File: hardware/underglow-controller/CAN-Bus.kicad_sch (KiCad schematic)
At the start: 4 parts, among them U3 SN65HVD230

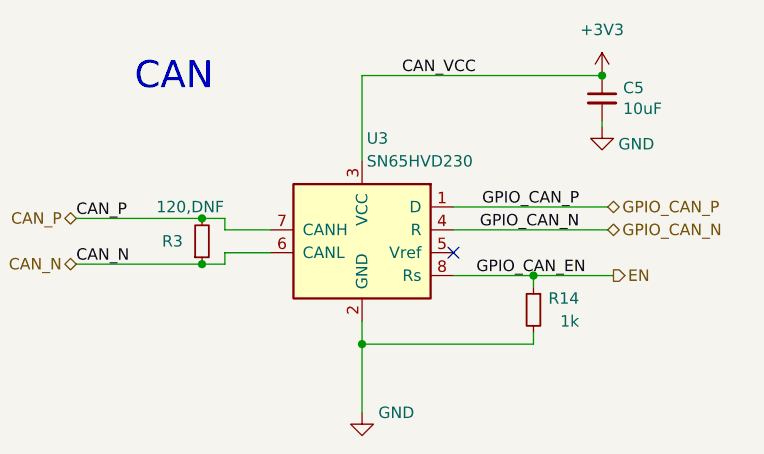
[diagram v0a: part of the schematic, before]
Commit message: add USB VIN
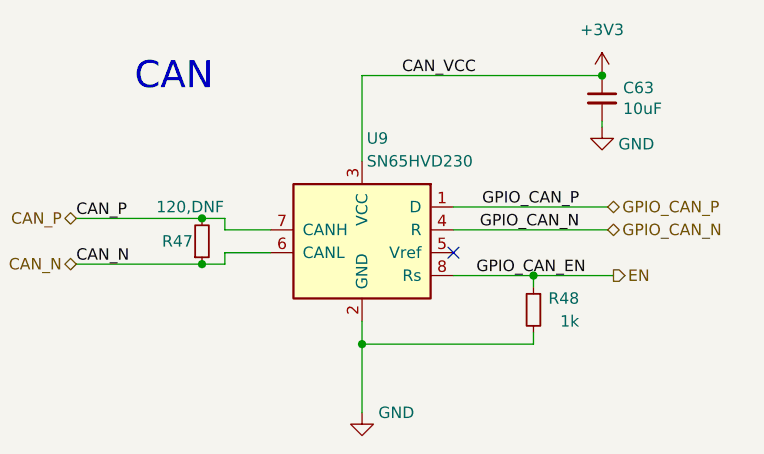
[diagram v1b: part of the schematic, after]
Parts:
- renumbered C5 to C63, R3 to R47, R14 to R48, U3 to U9
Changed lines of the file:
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@@
   (symbol (lib_id "power:+3V3") (at 127.635 43.815 0) (mirror y) (unit 1)
     (in_bom yes) (on_board yes) (fields_autoplaced)
-    (property "Reference" "#PWR018" (id 0) (at 127.635 47.625 0)
+    (property "Reference" "#PWR087" (id 0) (at 127.635 47.625 0)
       (effects (font (size 1.27 1.27)) hide)
     )
@@
   (symbol (lib_id "Device:R_Small") (at 83.185 62.23 0) (mirror x) (unit 1)
     (in_bom yes) (on_board yes)
-    (property "Reference" "R3" (id 0) (at 78.74 62.23 0)
+    (property "Reference" "R47" (id 0) (at 78.74 62.23 0)
       (effects (font (size 1.27 1.27)) (justify left))
     )
@@
   (symbol (lib_id "Device:C_Small") (at 127.635 46.355 0) (unit 1)
     (in_bom yes) (on_board yes)
-    (property "Reference" "C5" (id 0) (at 129.9718 45.1866 0)
+    (property "Reference" "C63" (id 0) (at 129.9718 45.1866 0)
       (effects (font (size 1.27 1.27)) (justify left))
     )
@@
   (symbol (lib_id "Device:R_Small") (at 120.015 69.85 0) (mirror y) (unit 1)
     (in_bom yes) (on_board yes)
-    (property "Reference" "R14" (id 0) (at 125.095 68.58 0)
+    (property "Reference" "R48" (id 0) (at 125.095 68.58 0)
       (effects (font (size 1.27 1.27)) (justify left))
     )
@@
   (symbol (lib_id "Interface_CAN_LIN:SN65HVD230") (at 100.965 60.96 0) (mirror y) (unit 1)
     (in_bom no) (on_board yes) (fields_autoplaced)
-    (property "Reference" "U3" (id 0) (at 101.4856 50.8 0)
+    (property "Reference" "U9" (id 0) (at 101.4856 50.8 0)
       (effects (font (size 1.27 1.27)) (justify right))
     )
@@
   (symbol (lib_id "power:GND") (at 127.635 49.53 0) (mirror y) (unit 1)
     (in_bom yes) (on_board yes)
-    (property "Reference" "#PWR019" (id 0) (at 127.635 55.88 0)
+    (property "Reference" "#PWR088" (id 0) (at 127.635 55.88 0)
       (effects (font (size 1.27 1.27)) hide)
     )
@@
   (symbol (lib_id "power:GND") (at 100.965 81.28 0) (mirror y) (unit 1)
     (in_bom yes) (on_board yes)
-    (property "Reference" "#PWR012" (id 0) (at 100.965 87.63 0)
+    (property "Reference" "#PWR089" (id 0) (at 100.965 87.63 0)
       (effects (font (size 1.27 1.27)) hide)
     )

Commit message: replace pmic
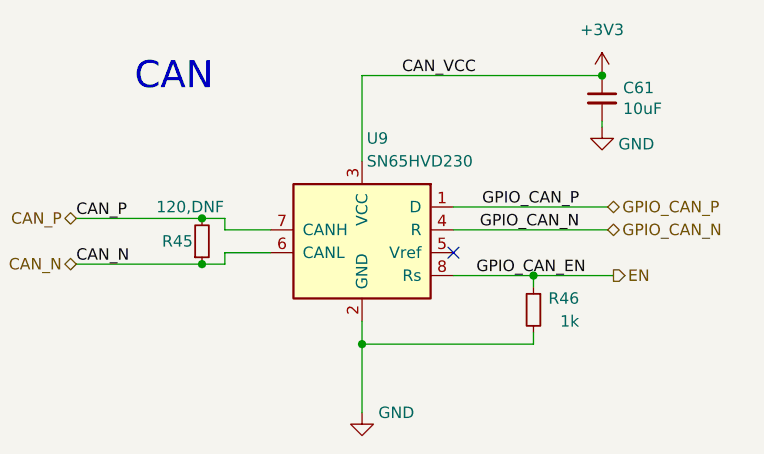
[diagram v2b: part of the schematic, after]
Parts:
- renumbered C63 to C61, R47 to R45, R48 to R46
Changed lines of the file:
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@@
   (symbol (lib_id "power:+3V3") (at 127.635 43.815 0) (mirror y) (unit 1)
     (in_bom yes) (on_board yes) (fields_autoplaced)
-    (property "Reference" "#PWR087" (id 0) (at 127.635 47.625 0)
+    (property "Reference" "#PWR088" (id 0) (at 127.635 47.625 0)
       (effects (font (size 1.27 1.27)) hide)
     )
@@
   (symbol (lib_id "Device:R_Small") (at 83.185 62.23 0) (mirror x) (unit 1)
     (in_bom yes) (on_board yes)
-    (property "Reference" "R47" (id 0) (at 78.74 62.23 0)
+    (property "Reference" "R45" (id 0) (at 78.74 62.23 0)
       (effects (font (size 1.27 1.27)) (justify left))
     )
@@
   (symbol (lib_id "Device:C_Small") (at 127.635 46.355 0) (unit 1)
     (in_bom yes) (on_board yes)
-    (property "Reference" "C63" (id 0) (at 129.9718 45.1866 0)
+    (property "Reference" "C61" (id 0) (at 129.9718 45.1866 0)
       (effects (font (size 1.27 1.27)) (justify left))
     )
@@
   (symbol (lib_id "Device:R_Small") (at 120.015 69.85 0) (mirror y) (unit 1)
     (in_bom yes) (on_board yes)
-    (property "Reference" "R48" (id 0) (at 125.095 68.58 0)
+    (property "Reference" "R46" (id 0) (at 125.095 68.58 0)
       (effects (font (size 1.27 1.27)) (justify left))
     )
@@
   (symbol (lib_id "power:GND") (at 127.635 49.53 0) (mirror y) (unit 1)
     (in_bom yes) (on_board yes)
-    (property "Reference" "#PWR088" (id 0) (at 127.635 55.88 0)
+    (property "Reference" "#PWR089" (id 0) (at 127.635 55.88 0)
       (effects (font (size 1.27 1.27)) hide)
     )
@@
   (symbol (lib_id "power:GND") (at 100.965 81.28 0) (mirror y) (unit 1)
     (in_bom yes) (on_board yes)
-    (property "Reference" "#PWR089" (id 0) (at 100.965 87.63 0)
+    (property "Reference" "#PWR090" (id 0) (at 100.965 87.63 0)
       (effects (font (size 1.27 1.27)) hide)
     )

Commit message: schematic rework progress
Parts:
- renumbered C61 to C59, U9 to U7
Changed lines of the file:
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@@
   (symbol (lib_id "power:+3V3") (at 127.635 43.815 0) (mirror y) (unit 1)
     (in_bom yes) (on_board yes) (fields_autoplaced)
-    (property "Reference" "#PWR088" (id 0) (at 127.635 47.625 0)
+    (property "Reference" "#PWR079" (id 0) (at 127.635 47.625 0)
       (effects (font (size 1.27 1.27)) hide)
     )
@@
   (symbol (lib_id "Device:C_Small") (at 127.635 46.355 0) (unit 1)
     (in_bom yes) (on_board yes)
-    (property "Reference" "C61" (id 0) (at 129.9718 45.1866 0)
+    (property "Reference" "C59" (id 0) (at 129.9718 45.1866 0)
       (effects (font (size 1.27 1.27)) (justify left))
     )
@@
   (symbol (lib_id "Interface_CAN_LIN:SN65HVD230") (at 100.965 60.96 0) (mirror y) (unit 1)
     (in_bom no) (on_board yes) (fields_autoplaced)
-    (property "Reference" "U9" (id 0) (at 101.4856 50.8 0)
+    (property "Reference" "U7" (id 0) (at 101.4856 50.8 0)
       (effects (font (size 1.27 1.27)) (justify right))
     )
@@
   (symbol (lib_id "power:GND") (at 127.635 49.53 0) (mirror y) (unit 1)
     (in_bom yes) (on_board yes)
-    (property "Reference" "#PWR089" (id 0) (at 127.635 55.88 0)
+    (property "Reference" "#PWR080" (id 0) (at 127.635 55.88 0)
       (effects (font (size 1.27 1.27)) hide)
     )
@@
   (symbol (lib_id "power:GND") (at 100.965 81.28 0) (mirror y) (unit 1)
     (in_bom yes) (on_board yes)
-    (property "Reference" "#PWR090" (id 0) (at 100.965 87.63 0)
+    (property "Reference" "#PWR081" (id 0) (at 100.965 87.63 0)
       (effects (font (size 1.27 1.27)) hide)
     )

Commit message: almost done picking components i think
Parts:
- renumbered R45 to R47, R46 to R48
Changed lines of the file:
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@@
   (symbol (lib_id "power:+3V3") (at 127.635 43.815 0) (mirror y) (unit 1)
     (in_bom yes) (on_board yes) (fields_autoplaced)
-    (property "Reference" "#PWR079" (id 0) (at 127.635 47.625 0)
+    (property "Reference" "#PWR080" (id 0) (at 127.635 47.625 0)
       (effects (font (size 1.27 1.27)) hide)
     )
@@
   (symbol (lib_id "Device:R_Small") (at 83.185 62.23 0) (mirror x) (unit 1)
     (in_bom yes) (on_board yes)
-    (property "Reference" "R45" (id 0) (at 78.74 62.23 0)
+    (property "Reference" "R47" (id 0) (at 78.74 62.23 0)
       (effects (font (size 1.27 1.27)) (justify left))
     )
@@
   (symbol (lib_id "Device:R_Small") (at 120.015 69.85 0) (mirror y) (unit 1)
     (in_bom yes) (on_board yes)
-    (property "Reference" "R46" (id 0) (at 125.095 68.58 0)
+    (property "Reference" "R48" (id 0) (at 125.095 68.58 0)
       (effects (font (size 1.27 1.27)) (justify left))
     )
@@
   (symbol (lib_id "power:GND") (at 127.635 49.53 0) (mirror y) (unit 1)
     (in_bom yes) (on_board yes)
-    (property "Reference" "#PWR080" (id 0) (at 127.635 55.88 0)
+    (property "Reference" "#PWR081" (id 0) (at 127.635 55.88 0)
       (effects (font (size 1.27 1.27)) hide)
     )
@@
   (symbol (lib_id "power:GND") (at 100.965 81.28 0) (mirror y) (unit 1)
     (in_bom yes) (on_board yes)
-    (property "Reference" "#PWR081" (id 0) (at 100.965 87.63 0)
+    (property "Reference" "#PWR082" (id 0) (at 100.965 87.63 0)
       (effects (font (size 1.27 1.27)) hide)
     )

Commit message: muh colored schematics
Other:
- note added: "CAN Transciever"
- note removed: "CAN"
- moved on the sheet: C59, R47, R48, U7

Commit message: antenna af
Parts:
- renumbered C59 to C56, R47 to R46, R48 to R47, U7 to U8
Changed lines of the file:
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@@
   (symbol (lib_id "Device:R_Small") (at 80.645 68.58 0) (mirror x) (unit 1)
     (in_bom yes) (on_board yes)
-    (property "Reference" "R47" (id 0) (at 76.2 68.58 0)
+    (property "Reference" "R46" (id 0) (at 76.2 68.58 0)
       (effects (font (size 1.27 1.27)) (justify left))
     )
@@
   (symbol (lib_id "Device:C_Small") (at 125.095 52.705 0) (unit 1)
     (in_bom yes) (on_board yes)
-    (property "Reference" "C59" (id 0) (at 127.4318 51.5366 0)
+    (property "Reference" "C56" (id 0) (at 127.4318 51.5366 0)
       (effects (font (size 1.27 1.27)) (justify left))
     )
@@
   (symbol (lib_id "Device:R_Small") (at 117.475 76.2 0) (mirror y) (unit 1)
     (in_bom yes) (on_board yes)
-    (property "Reference" "R48" (id 0) (at 122.555 74.93 0)
+    (property "Reference" "R47" (id 0) (at 122.555 74.93 0)
       (effects (font (size 1.27 1.27)) (justify left))
     )
@@
   (symbol (lib_id "Interface_CAN_LIN:SN65HVD230") (at 98.425 67.31 0) (mirror y) (unit 1)
     (in_bom no) (on_board yes) (fields_autoplaced)
-    (property "Reference" "U7" (id 0) (at 98.9456 57.15 0)
+    (property "Reference" "U8" (id 0) (at 98.9456 57.15 0)
       (effects (font (size 1.27 1.27)) (justify right))
     )

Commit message: pizz
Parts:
- renumbered C56 to C59
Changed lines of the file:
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@@
   (symbol (lib_id "power:+3V3") (at 125.095 50.165 0) (mirror y) (unit 1)
     (in_bom yes) (on_board yes) (fields_autoplaced)
-    (property "Reference" "#PWR080" (id 0) (at 125.095 53.975 0)
+    (property "Reference" "#PWR081" (id 0) (at 125.095 53.975 0)
       (effects (font (size 1.27 1.27)) hide)
     )
@@
   (symbol (lib_id "Device:C_Small") (at 125.095 52.705 0) (unit 1)
     (in_bom yes) (on_board yes)
-    (property "Reference" "C56" (id 0) (at 127.4318 51.5366 0)
+    (property "Reference" "C59" (id 0) (at 127.4318 51.5366 0)
       (effects (font (size 1.27 1.27)) (justify left))
     )
@@
   (symbol (lib_id "power:GND") (at 125.095 55.88 0) (mirror y) (unit 1)
     (in_bom yes) (on_board yes)
-    (property "Reference" "#PWR081" (id 0) (at 125.095 62.23 0)
+    (property "Reference" "#PWR082" (id 0) (at 125.095 62.23 0)
       (effects (font (size 1.27 1.27)) hide)
     )
@@
   (symbol (lib_id "power:GND") (at 98.425 87.63 0) (mirror y) (unit 1)
     (in_bom yes) (on_board yes)
-    (property "Reference" "#PWR082" (id 0) (at 98.425 93.98 0)
+    (property "Reference" "#PWR083" (id 0) (at 98.425 93.98 0)
       (effects (font (size 1.27 1.27)) hide)
     )

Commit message: aaaaa
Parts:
- renumbered C59 to C44, R46 to R30, R47 to R31, U8 to U9
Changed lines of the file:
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@@
   (symbol (lib_id "power:+3V3") (at 125.095 50.165 0) (mirror y) (unit 1)
     (in_bom yes) (on_board yes) (fields_autoplaced)
-    (property "Reference" "#PWR081" (id 0) (at 125.095 53.975 0)
+    (property "Reference" "#PWR067" (id 0) (at 125.095 53.975 0)
       (effects (font (size 1.27 1.27)) hide)
     )
@@
   (symbol (lib_id "Device:R_Small") (at 80.645 68.58 0) (mirror x) (unit 1)
     (in_bom yes) (on_board yes)
-    (property "Reference" "R46" (id 0) (at 76.2 68.58 0)
+    (property "Reference" "R30" (id 0) (at 76.2 68.58 0)
       (effects (font (size 1.27 1.27)) (justify left))
     )
@@
   (symbol (lib_id "Device:C_Small") (at 125.095 52.705 0) (unit 1)
     (in_bom yes) (on_board yes)
-    (property "Reference" "C59" (id 0) (at 127.4318 51.5366 0)
+    (property "Reference" "C44" (id 0) (at 127.4318 51.5366 0)
       (effects (font (size 1.27 1.27)) (justify left))
     )
@@
   (symbol (lib_id "Device:R_Small") (at 117.475 76.2 0) (mirror y) (unit 1)
     (in_bom yes) (on_board yes)
-    (property "Reference" "R47" (id 0) (at 122.555 74.93 0)
+    (property "Reference" "R31" (id 0) (at 122.555 74.93 0)
       (effects (font (size 1.27 1.27)) (justify left))
     )
@@
   (symbol (lib_id "Interface_CAN_LIN:SN65HVD230") (at 98.425 67.31 0) (mirror y) (unit 1)
     (in_bom no) (on_board yes) (fields_autoplaced)
-    (property "Reference" "U8" (id 0) (at 98.9456 57.15 0)
+    (property "Reference" "U9" (id 0) (at 98.9456 57.15 0)
       (effects (font (size 1.27 1.27)) (justify right))
     )
@@
   (symbol (lib_id "power:GND") (at 125.095 55.88 0) (mirror y) (unit 1)
     (in_bom yes) (on_board yes)
-    (property "Reference" "#PWR082" (id 0) (at 125.095 62.23 0)
+    (property "Reference" "#PWR068" (id 0) (at 125.095 62.23 0)
       (effects (font (size 1.27 1.27)) hide)
     )
@@
   (symbol (lib_id "power:GND") (at 98.425 87.63 0) (mirror y) (unit 1)
     (in_bom yes) (on_board yes)
-    (property "Reference" "#PWR083" (id 0) (at 98.425 93.98 0)
+    (property "Reference" "#PWR069" (id 0) (at 98.425 93.98 0)
       (effects (font (size 1.27 1.27)) hide)
     )
